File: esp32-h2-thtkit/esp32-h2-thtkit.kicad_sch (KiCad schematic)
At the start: 25 parts, among them J1 PIN_GROUP_1, J2 PIN_GROUP_2, J3 UART, J6 PIN_GROUP_3, U2 ESP32-H2, U3 MIC5219-3.3YM5, Y1 32MHz ±10ppm CL8pF

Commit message: Use connectors without silkscreen to place them right on the corner
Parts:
- J1, J2: footprint Connector_PinHeader_2.54mm:PinHeader_1x06_P2.54mm_Vertical -> PCM_SKC_Connector_PinHeader_2.54mm:PinHeader_1x06_P2.54mm_Vertical_NoSilk
- J6: footprint Connector_PinHeader_2.54mm:PinHeader_1x04_P2.54mm_Vertical -> PCM_SKC_Connector_PinHeader_2.54mm:PinHeader_1x04_P2.54mm_Vertical_NoSilk
- U2: footprint PCM_SKC_MCU_Espressif:TQFN_32_1EP_4x4mm_P0.4mm_EP2.4x2.4mm_Compact -> SKC_MCU_Espressif:TQFN_32_1EP_4x4mm_P0.4mm_EP2.6x2.6mm_Standard
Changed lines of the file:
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@@
 			)
 		)
-		(property "Footprint" "PCM_SKC_MCU_Espressif:TQFN_32_1EP_4x4mm_P0.4mm_EP2.4x2.4mm_Compact"
+		(property "Footprint" "SKC_MCU_Espressif:TQFN_32_1EP_4x4mm_P0.4mm_EP2.6x2.6mm_Standard"
 			(at 97.79 74.93 0)
 			(effects
@@
 			)
 		)
-		(property "Datasheet" "${KICADX_LIBS}/datasheets/esp32-h2.pdf"
+		(property "Datasheet" "https://cdn.jsdelivr.net/gh/sivakov512/kicad-library@master/datasheets/MCU/Espressif/Espressif_ESP32-H2.pdf"
 			(at 97.79 74.93 0)
 			(effects
@@
 			)
 		)
-		(property "Footprint" "Connector_PinHeader_2.54mm:PinHeader_1x06_P2.54mm_Vertical"
+		(property "Footprint" "PCM_SKC_Connector_PinHeader_2.54mm:PinHeader_1x06_P2.54mm_Vertical_NoSilk"
 			(at 226.06 147.32 0)
 			(effects
@@
 			)
 		)
-		(property "Footprint" "Connector_PinHeader_2.54mm:PinHeader_1x04_P2.54mm_Vertical"
+		(property "Footprint" "PCM_SKC_Connector_PinHeader_2.54mm:PinHeader_1x04_P2.54mm_Vertical_NoSilk"
 			(at 266.7 142.24 0)
 			(effects
@@
 			)
 		)
-		(property "Footprint" "Connector_PinHeader_2.54mm:PinHeader_1x06_P2.54mm_Vertical"
+		(property "Footprint" "PCM_SKC_Connector_PinHeader_2.54mm:PinHeader_1x06_P2.54mm_Vertical_NoSilk"
 			(at 246.38 147.32 0)
 			(effects

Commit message: Full schematic and PCB layout for esp32-h2 tht kit
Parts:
- J1: value PIN_GROUP_1 -> PIN_GROUP_2; LCSC PN C37208 -> (none); now left out of the parts list
- J2: value PIN_GROUP_2 -> PIN_GROUP_1; LCSC PN C37208 -> (none); now left out of the parts list
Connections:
- net GND: now also J1.1 (Pin_1); no longer J2.1 (Pin_1)
- net VIN: now also J2.1 (Pin_1); no longer J1.1 (Pin_1)
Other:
- moved on the sheet: J1, J2
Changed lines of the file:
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@@
 	)
 	(label "GPIO1"
-		(at 220.98 147.32 180)
+		(at 241.3 147.32 180)
 		(effects
 			(font
@@
 	)
 	(label "GPIO27"
-		(at 241.3 139.7 180)
+		(at 220.98 139.7 180)
 		(effects
 			(font
@@
 	)
 	(label "GPIO11"
-		(at 220.98 139.7 180)
+		(at 241.3 139.7 180)
 		(effects
 			(font
@@
 	)
 	(label "GPIO22"
-		(at 241.3 147.32 180)
+		(at 220.98 147.32 180)
 		(effects
 			(font
@@
 	)
 	(label "GPIO25"
-		(at 241.3 144.78 180)
+		(at 220.98 144.78 180)
 		(effects
 			(font
@@
 	)
 	(label "GPIO26"
-		(at 241.3 142.24 180)
+		(at 220.98 142.24 180)
 		(effects
 			(font
@@
 	)
 	(label "GPIO12"
-		(at 241.3 149.86 180)
+		(at 220.98 149.86 180)
 		(effects
 			(font
@@
 	)
 	(label "GPIO8"
-		(at 220.98 144.78 180)
+		(at 241.3 144.78 180)
 		(effects
 			(font
@@
 	)
 	(label "GPIO0"
-		(at 220.98 149.86 180)
+		(at 241.3 149.86 180)
 		(effects
 			(font
@@
 	)
 	(label "GPIO10"
-		(at 220.98 142.24 180)
+		(at 241.3 142.24 180)
 		(effects
 			(font
@@
 	(symbol
 		(lib_id "Connector:Conn_01x06_Pin")
-		(at 226.06 147.32 180)
-		(unit 1)
-		(exclude_from_sim no)
-		(in_bom yes)
+		(at 246.38 147.32 180)
+		(unit 1)
+		(exclude_from_sim no)
+		(in_bom no)
 		(on_board yes)
 		(dnp no)
 		(property "Reference" "J1"
-			(at 226.06 133.35 0)
-			(effects
-				(font
-					(size 1.27 1.27)
-				)
-			)
-		)
-		(property "Value" "PIN_GROUP_1"
-			(at 226.06 135.89 0)
+			(at 246.38 133.35 0)
+			(effects
+				(font
+					(size 1.27 1.27)
+				)
+			)
+		)
+		(property "Value" "PIN_GROUP_2"
+			(at 246.38 135.89 0)
 			(effects
 				(font
@@
 		)
 		(property "Footprint" "PCM_SKC_Connector_PinHeader_2.54mm:PinHeader_1x06_P2.54mm_Vertical_NoSilk"
-			(at 226.06 147.32 0)
+			(at 246.38 147.32 0)
 			(effects
 				(font
@@
 		)
 		(property "Datasheet" "~"
-			(at 226.06 147.32 0)
+			(at 246.38 147.32 0)
 			(effects
 				(font
@@
 		)
 		(property "Description" "Generic connector, single row, 01x06, script generated"
-			(at 226.06 147.32 0)
-			(effects
-				(font
-					(size 1.27 1.27)
-				)
-				(hide yes)
-			)
-		)
-		(property "LCSC PN" "C37208"
-			(at 226.06 147.32 0)
+			(at 246.38 147.32 0)
+			(effects
+				(font
+					(size 1.27 1.27)
+				)
+				(hide yes)
+			)
+		)
+		(property "LCSC PN" ""
+			(at 246.38 147.32 0)
 			(effects
 				(font
@@
 	(symbol
 		(lib_id "Connector:Conn_01x06_Pin")
-		(at 246.38 147.32 180)
-		(unit 1)
-		(exclude_from_sim no)
-		(in_bom yes)
+		(at 226.06 147.32 180)
+		(unit 1)
+		(exclude_from_sim no)
+		(in_bom no)
 		(on_board yes)
 		(dnp no)
 		(property "Reference" "J2"
-			(at 246.38 133.35 0)
-			(effects
-				(font
-					(size 1.27 1.27)
-				)
-			)
-		)
-		(property "Value" "PIN_GROUP_2"
-			(at 246.38 135.89 0)
+			(at 226.06 133.35 0)
+			(effects
+				(font
+					(size 1.27 1.27)
+				)
+			)
+		)
+		(property "Value" "PIN_GROUP_1"
+			(at 226.06 135.89 0)
 			(effects
 				(font
@@
 		)
 		(property "Footprint" "PCM_SKC_Connector_PinHeader_2.54mm:PinHeader_1x06_P2.54mm_Vertical_NoSilk"
-			(at 246.38 147.32 0)
+			(at 226.06 147.32 0)
 			(effects
 				(font
@@
 		)
 		(property "Datasheet" "~"
-			(at 246.38 147.32 0)
+			(at 226.06 147.32 0)
 			(effects
 				(font
@@
 		)
 		(property "Description" "Generic connector, single row, 01x06, script generated"
-			(at 246.38 147.32 0)
-			(effects
-				(font
-					(size 1.27 1.27)
-				)
-				(hide yes)
-			)
-		)
-		(property "LCSC PN" "C37208"
-			(at 246.38 147.32 0)
-			(effects
-				(font
+			(at 226.06 147.32 0)
+			(effects
+				(font
+					(size 1.27 1.27)
+				)
+				(hide yes)
+			)
+		)
+		(property "LCSC PN" ""
+			(at 226.06 147.32 0)
+			(effects
+				(font

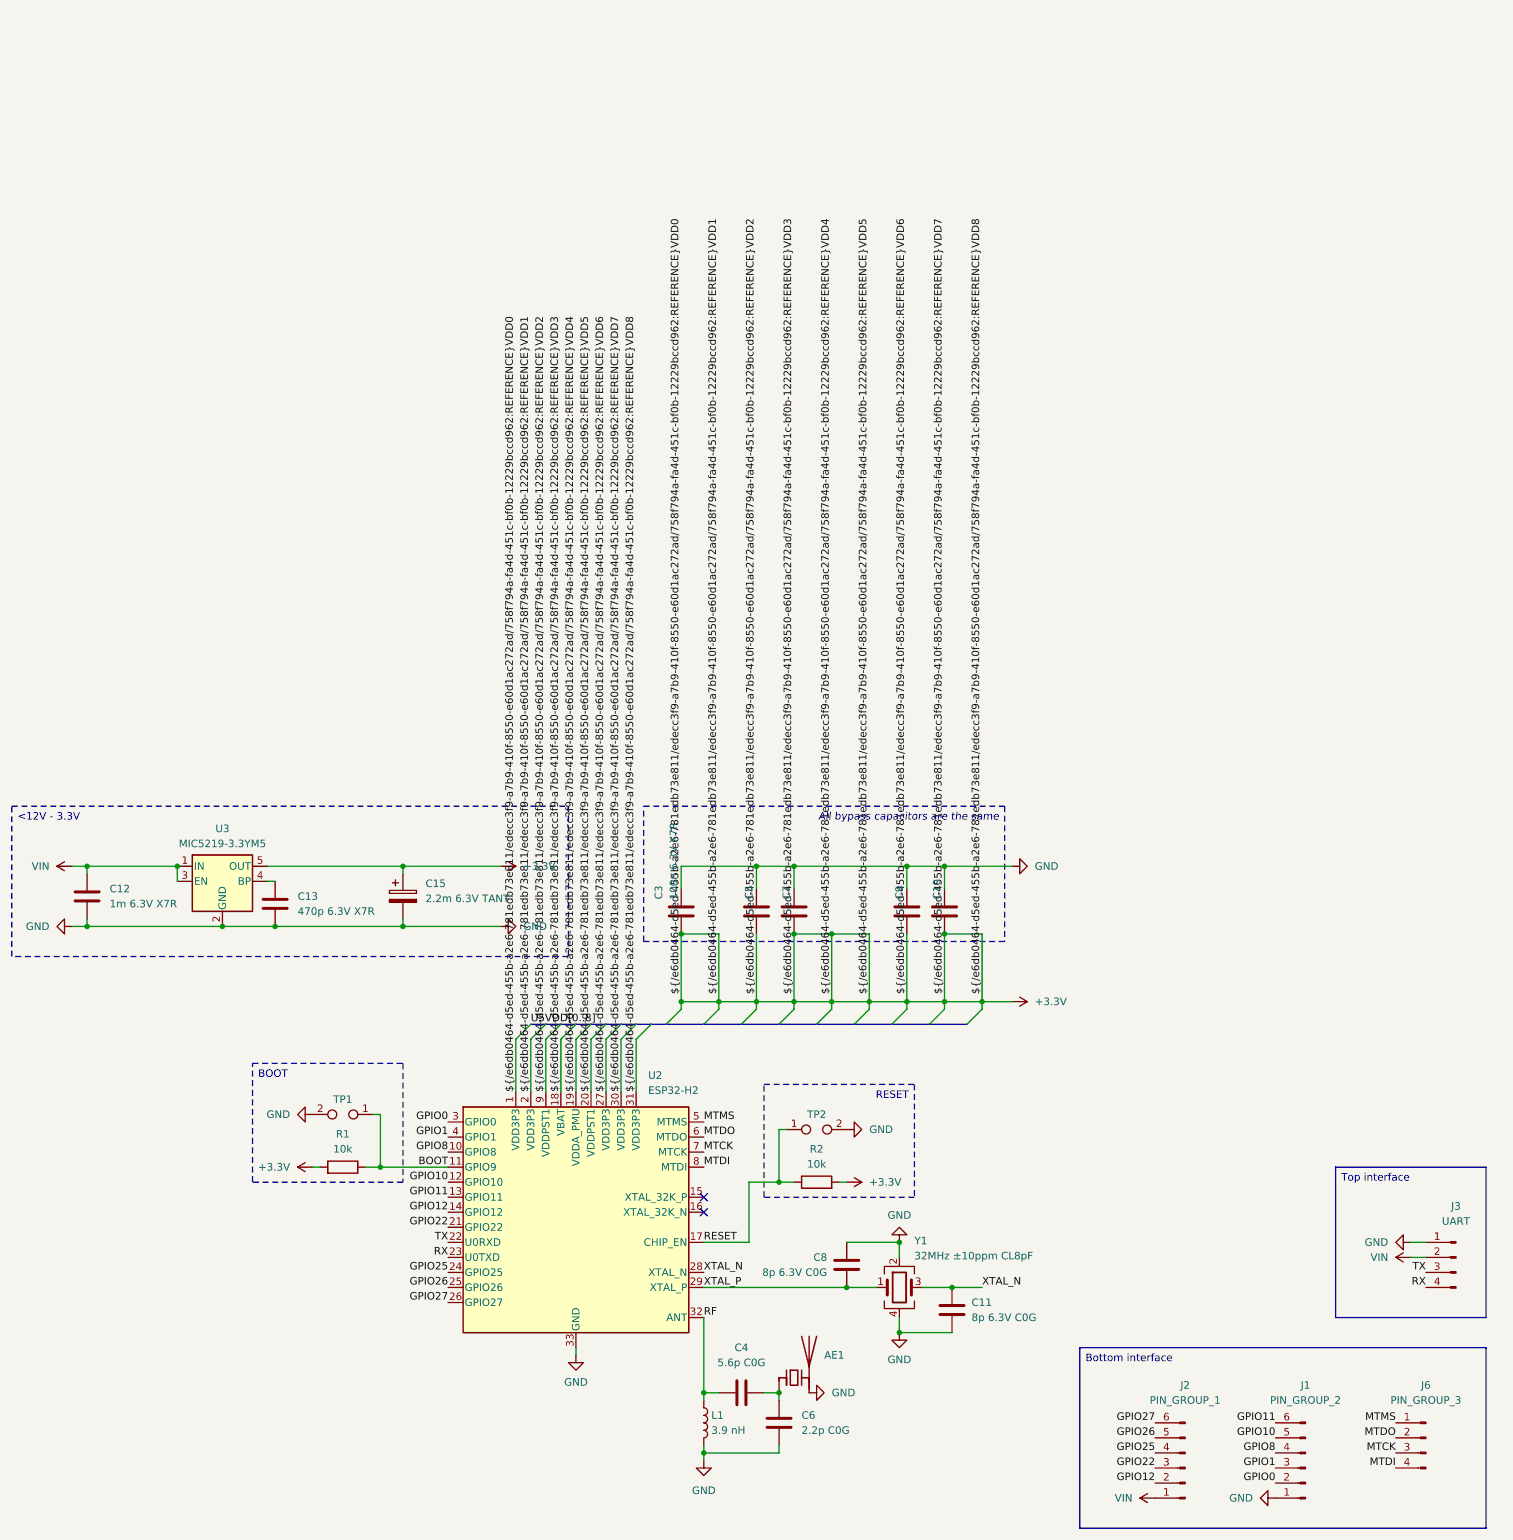
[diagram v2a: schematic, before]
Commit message: Added 32k crystal, updated footprint, few rearranges
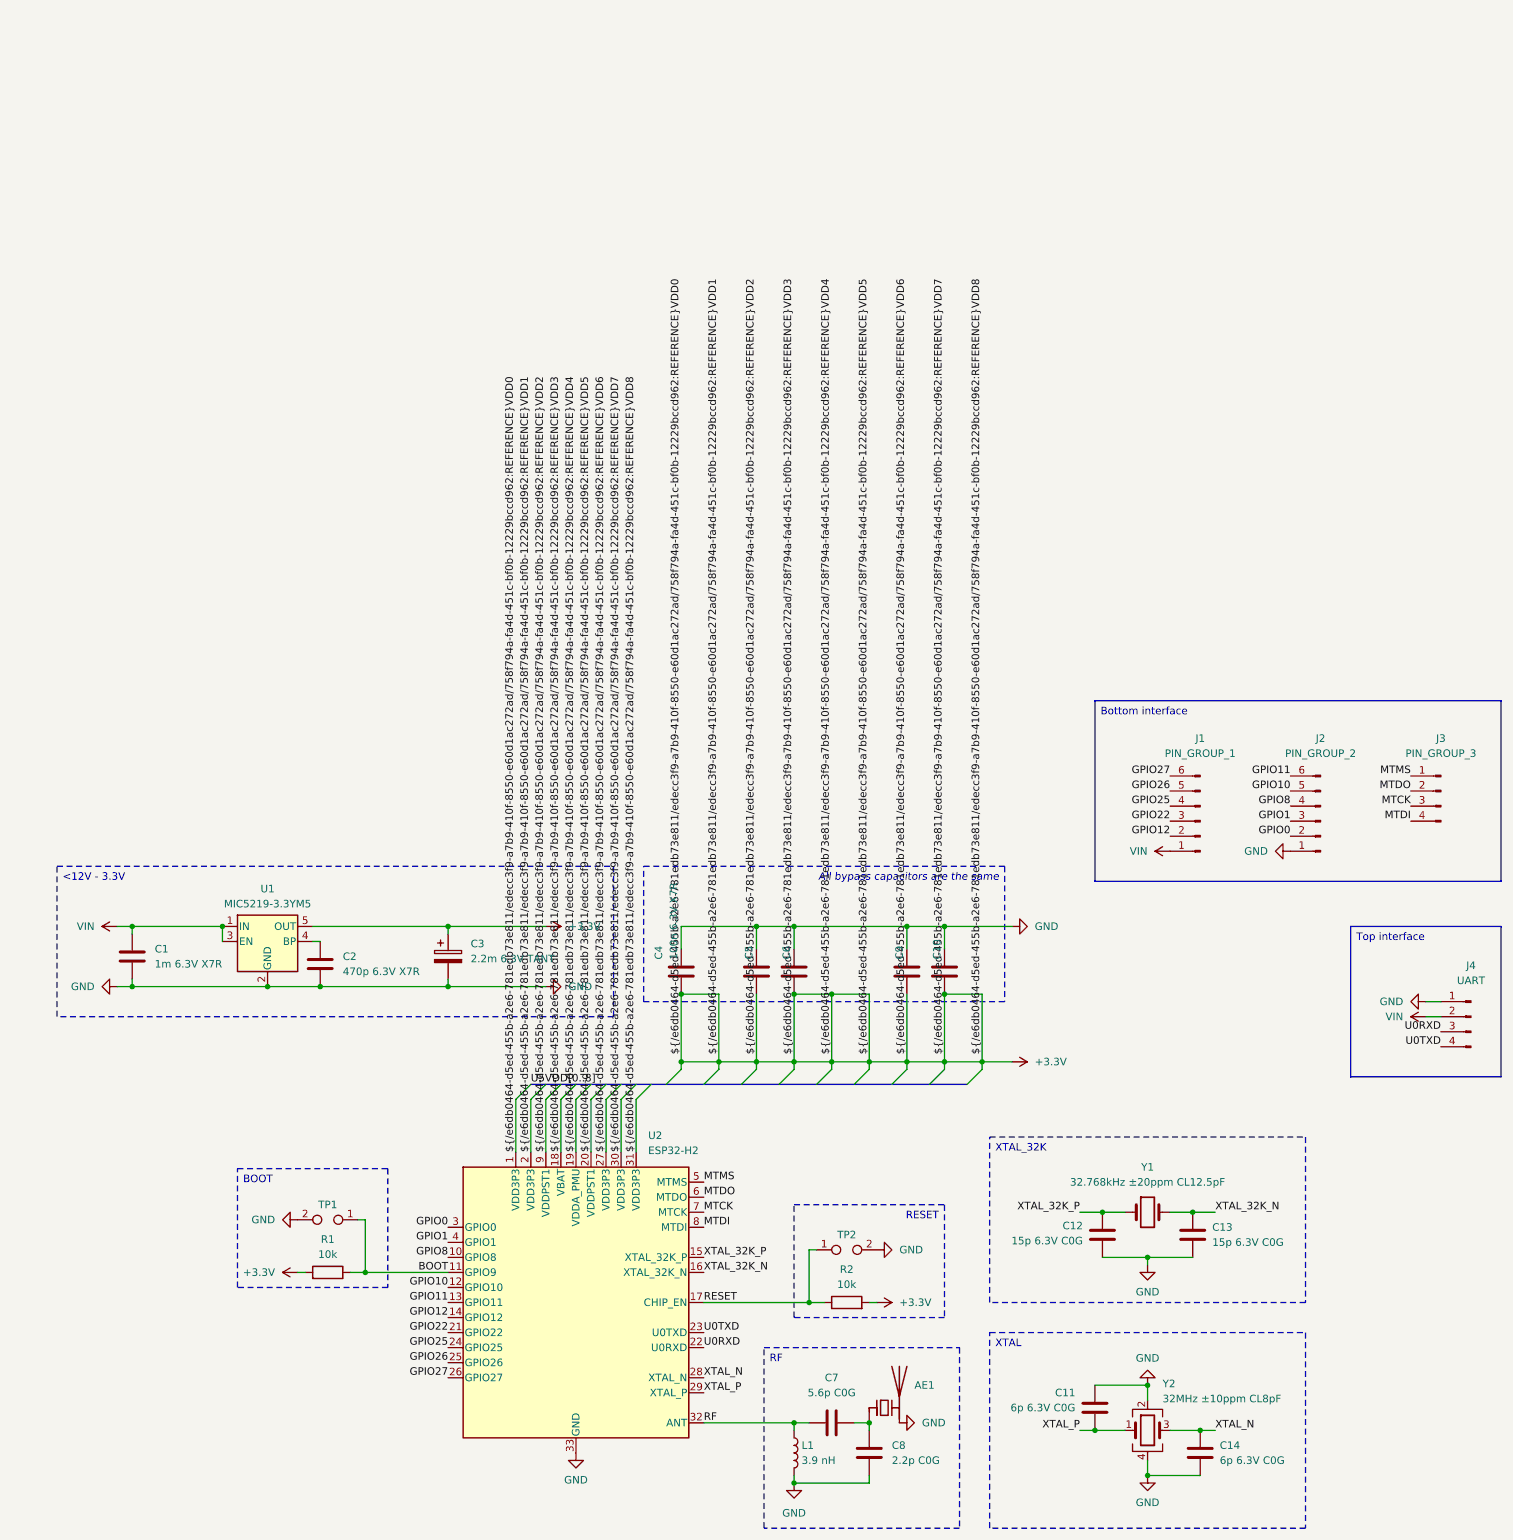
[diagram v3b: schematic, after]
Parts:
- added C12, C13: 15p 6.3V C0G, Capacitor_SMD:C_0201_0603Metric, symbol Device:C
- added Y1: 32.768kHz ±20ppm CL12.5pF, Crystal:Crystal_SMD_2012-2Pin_2.0x1.2mm, symbol Device:Crystal
- C11: renamed from C8; value 8p 6.3V C0G -> 6p 6.3V C0G; LCSC PN C237455 -> C161434
- C14: renamed from C11; value 8p 6.3V C0G -> 6p 6.3V C0G
- Y2: renamed from Y1; footprint Crystal:Crystal_SMD_2016-4Pin_2.0x1.6mm -> PCM_SKC_Crystals:Crystal_SMD_1612-4Pin_1.6x1.2mm; LCSC PN C2965582 -> C7301921
- renumbered C12 to C1, C13 to C2, C15 to C3, C3 to C4, C7 to C6, C4 to C7, C6 to C8, J2 to J1, J1 to J2, J6 to J3, J3 to J4, U3 to U1
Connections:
- net GND: now also C12.1, C13.1
- net XTAL_32K_P: now reaches U2.15 (XTAL_32K_P)
- net XTAL_32K_P: now also C12.2, Y1.1
- net XTAL_32K_N: now reaches U2.16 (XTAL_32K_N)
- net XTAL_32K_N: now also C13.2, Y1.2
- net RX renamed U0TXD
- net TX renamed U0RXD
- no-connect marks 2 -> 0
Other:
- moved on the sheet: AE1, C1, C10, C11, C14, C2, C3, C4, C5, C6, C7, C8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

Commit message: Improve layout to make better SPI routes
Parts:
- removed J4: UART, Connector_PinHeader_2.54mm:PinHeader_1x04_P2.54mm_Vertical, symbol Connector:Conn_01x04_Pin
- removed TP1, TP2: TestPoint_2Pole, TestPoint:TestPoint_Pad_D1.0mm, symbol Connector:TestPoint_2Pole
- added J4: UART, PCM_SKC_Connector_PinHeader_2.54mm:PinHeader_1x02_P2.54mm_Vertical_NoSilk, symbol Connector:Conn_01x02_Pin
- added TP1, TP2: TestPoint, TestPoint:TestPoint_Pad_D1.0mm, symbol Connector:TestPoint
- AE1: footprint PCM_SKC_Antennas_SMD:Antenna_PCB_Espressif_2.4GHz_Left -> PCM_SKC_Antennas_SMD:Antenna_PCB_Espressif_2.4GHz_Right
- J2: value PIN_GROUP_2 -> PIN_GROUP_3
- J3: value PIN_GROUP_3 -> PIN_GROUP_2
- U2: footprint SKC_MCU_Espressif:TQFN_32_1EP_4x4mm_P0.4mm_EP2.6x2.6mm_Standard -> PCM_SKC_MCU_Espressif:TQFN_32_1EP_4x4mm_P0.4mm_EP2.4x2.4mm_Compact
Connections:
- net BOOT: now also TP1.1
- net GND: now also J2.2 (Pin_2); no longer J2.1 (Pin_1)
- net GPIO0: now also J1.1 (Pin_1); no longer J2.2 (Pin_2)
- net GPIO1: now also J1.2 (Pin_2); no longer J2.3 (Pin_3)
- net GPIO10: now also J3.2 (Pin_2); no longer J2.5 (Pin_5)
- net GPIO11: now also J3.3 (Pin_3); no longer J2.6 (Pin_6)
- net GPIO12: now also J3.4 (Pin_4); no longer J1.2 (Pin_2)
- net GPIO22: now also J2.6 (Pin_6); no longer J1.3 (Pin_3)
- net GPIO25: now also J2.5 (Pin_5); no longer J1.4 (Pin_4)
- net GPIO26: now also J2.4 (Pin_4); no longer J1.5 (Pin_5)
- net GPIO27: now also J2.3 (Pin_3); no longer J1.6 (Pin_6)
- net GPIO8: now also J3.1 (Pin_1); no longer J2.4 (Pin_4)
- net MTCK: now also J1.5 (Pin_5); no longer J3.3 (Pin_3)
- net MTDI: now also J1.6 (Pin_6); no longer J3.4 (Pin_4)
- net MTDO: now also J1.4 (Pin_4); no longer J3.2 (Pin_2)
- net MTMS: now also J1.3 (Pin_3); no longer J3.1 (Pin_1)
- net RESET: now also TP2.1
- net U0RXD: now also J4.2 (Pin_2)
- net U0TXD: now also J4.1 (Pin_1)
- net VIN: now also J2.1 (Pin_1); no longer J1.1 (Pin_1)
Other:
- moved on the sheet: J1, J2

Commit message: Change some manufacturing related attributes
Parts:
- TP1, TP2: now left out of the parts list
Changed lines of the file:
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@@
 		(unit 1)
 		(exclude_from_sim no)
-		(in_bom yes)
+		(in_bom no)
 		(on_board yes)
 		(dnp no)
@@
 		(unit 1)
 		(exclude_from_sim no)
-		(in_bom yes)
-		(on_board yes)
-		(dnp no)
+		(in_bom no)
+		(on_board yes)
+		(dnp no)

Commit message: Make devkits cheaper by using 0402 components instead of 0201
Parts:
- C11: value 6p 6.3V C0G -> 15p 6.3V C0G; footprint Capacitor_SMD:C_0201_0603Metric -> Capacitor_SMD:C_0402_1005Metric; LCSC PN C161434 -> C1548
- C12: value 15p 6.3V C0G -> 25p 6.3V C0G; footprint Capacitor_SMD:C_0201_0603Metric -> Capacitor_SMD:C_0402_1005Metric; LCSC PN C22374851 -> C1556
- C13: value 15p 6.3V C0G -> 25p 6.3V C0G; footprint Capacitor_SMD:C_0201_0603Metric -> Capacitor_SMD:C_0402_1005Metric; LCSC PN C237455 -> C1556
- C14: value 6p 6.3V C0G -> 15p 6.3V C0G; footprint Capacitor_SMD:C_0201_0603Metric -> Capacitor_SMD:C_0402_1005Metric; LCSC PN C237455 -> C1548
- C2: footprint Capacitor_SMD:C_0201_0603Metric -> Capacitor_SMD:C_0402_1005Metric; LCSC PN C694489 -> C1537
- C7: footprint Capacitor_SMD:C_0201_0603Metric -> Capacitor_SMD:C_0402_1005Metric; LCSC PN C85914 -> C1574
- C8: footprint Capacitor_SMD:C_0201_0603Metric -> Capacitor_SMD:C_0402_1005Metric; LCSC PN C710732 -> C1559
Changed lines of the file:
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@@
 		(title "ESP32-H2-THTKIT")
 		(date "2025-05-28")
-		(rev "1.0.0")
+		(rev "1.0.1")
 		(company "SIVAKOV.TECH")
 	)
@@
 			)
 		)
-		(property "Value" "6p 6.3V C0G"
+		(property "Value" "15p 6.3V C0G"
 			(at 207.518 137.16 0)
 			(effects
@@
 			)
 		)
-		(property "Footprint" "Capacitor_SMD:C_0201_0603Metric"
+		(property "Footprint" "Capacitor_SMD:C_0402_1005Metric"
 			(at 209.8548 133.35 0)
 			(effects
@@
 			)
 		)
-		(property "LCSC PN" "C161434"
+		(property "LCSC PN" "C1548"
 			(at 210.82 137.16 0)
 			(effects
@@
 			)
 		)
-		(property "Footprint" "Capacitor_SMD:C_0201_0603Metric"
+		(property "Footprint" "Capacitor_SMD:C_0402_1005Metric"
 			(at 171.7548 140.97 0)
 			(effects
@@
 			)
 		)
-		(property "LCSC PN" "C710732"
+		(property "LCSC PN" "C1559"
 			(at 172.72 144.78 0)
 			(effects
@@
 			)
 		)
-		(property "Footprint" "Capacitor_SMD:C_0201_0603Metric"
+		(property "Footprint" "Capacitor_SMD:C_0402_1005Metric"
 			(at 79.0448 58.42 0)
 			(effects
@@
 			)
 		)
-		(property "LCSC PN" "C694489"
+		(property "LCSC PN" "C1537"
 			(at 80.01 62.23 0)
 			(effects
@@
 			)
 		)
-		(property "Footprint" "Capacitor_SMD:C_0201_0603Metric"
+		(property "Footprint" "Capacitor_SMD:C_0402_1005Metric"
 			(at 162.56 140.6652 0)
 			(effects
@@
 			)
 		)
-		(property "LCSC PN" "C85914"
+		(property "LCSC PN" "C1574"
 			(at 166.37 139.7 90)
 			(effects
@@
 			)
 		)
-		(property "Value" "6p 6.3V C0G"
+		(property "Value" "15p 6.3V C0G"
 			(at 231.902 146.05 0)
 			(effects
@@
 			)
 		)
-		(property "Footprint" "Capacitor_SMD:C_0201_0603Metric"
+		(property "Footprint" "Capacitor_SMD:C_0402_1005Metric"
 			(at 227.6348 140.97 0)
 			(effects
@@
 			)
 		)
-		(property "LCSC PN" "C237455"
+		(property "LCSC PN" "C1548"
 			(at 228.6 144.78 0)
 			(effects
@@
 			)
 		)
-		(property "Value" "15p 6.3V C0G"
+		(property "Value" "25p 6.3V C0G"
 			(at 208.788 108.966 0)
 			(effects
@@
 			)
 		)
-		(property "Footprint" "Capacitor_SMD:C_0201_0603Metric"
+		(property "Footprint" "Capacitor_SMD:C_0402_1005Metric"
 			(at 211.1248 104.14 0)
 			(effects
@@
 			)
 		)
-		(property "LCSC PN" "C22374851"
+		(property "LCSC PN" "C1556"
 			(at 212.09 107.95 0)
 			(effects
@@
 			)
 		)
-		(property "Value" "15p 6.3V C0G"
+		(property "Value" "25p 6.3V C0G"
 			(at 230.632 109.22 0)
 			(effects
@@
 			)
 		)
-		(property "Footprint" "Capacitor_SMD:C_0201_0603Metric"
+		(property "Footprint" "Capacitor_SMD:C_0402_1005Metric"
 			(at 226.3648 104.14 0)
 			(effects
@@
 			)
 		)
-		(property "LCSC PN" "C237455"
+		(property "LCSC PN" "C1556"
 			(at 227.33 107.95 0)
 			(effects
